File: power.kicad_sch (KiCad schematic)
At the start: 28 parts, among them J1 USBC, Q1 2N7002, SW3 PWR_ON, U2 LM3670MF, U5 MCP73831-3-OT, U6 MAX17043G+T

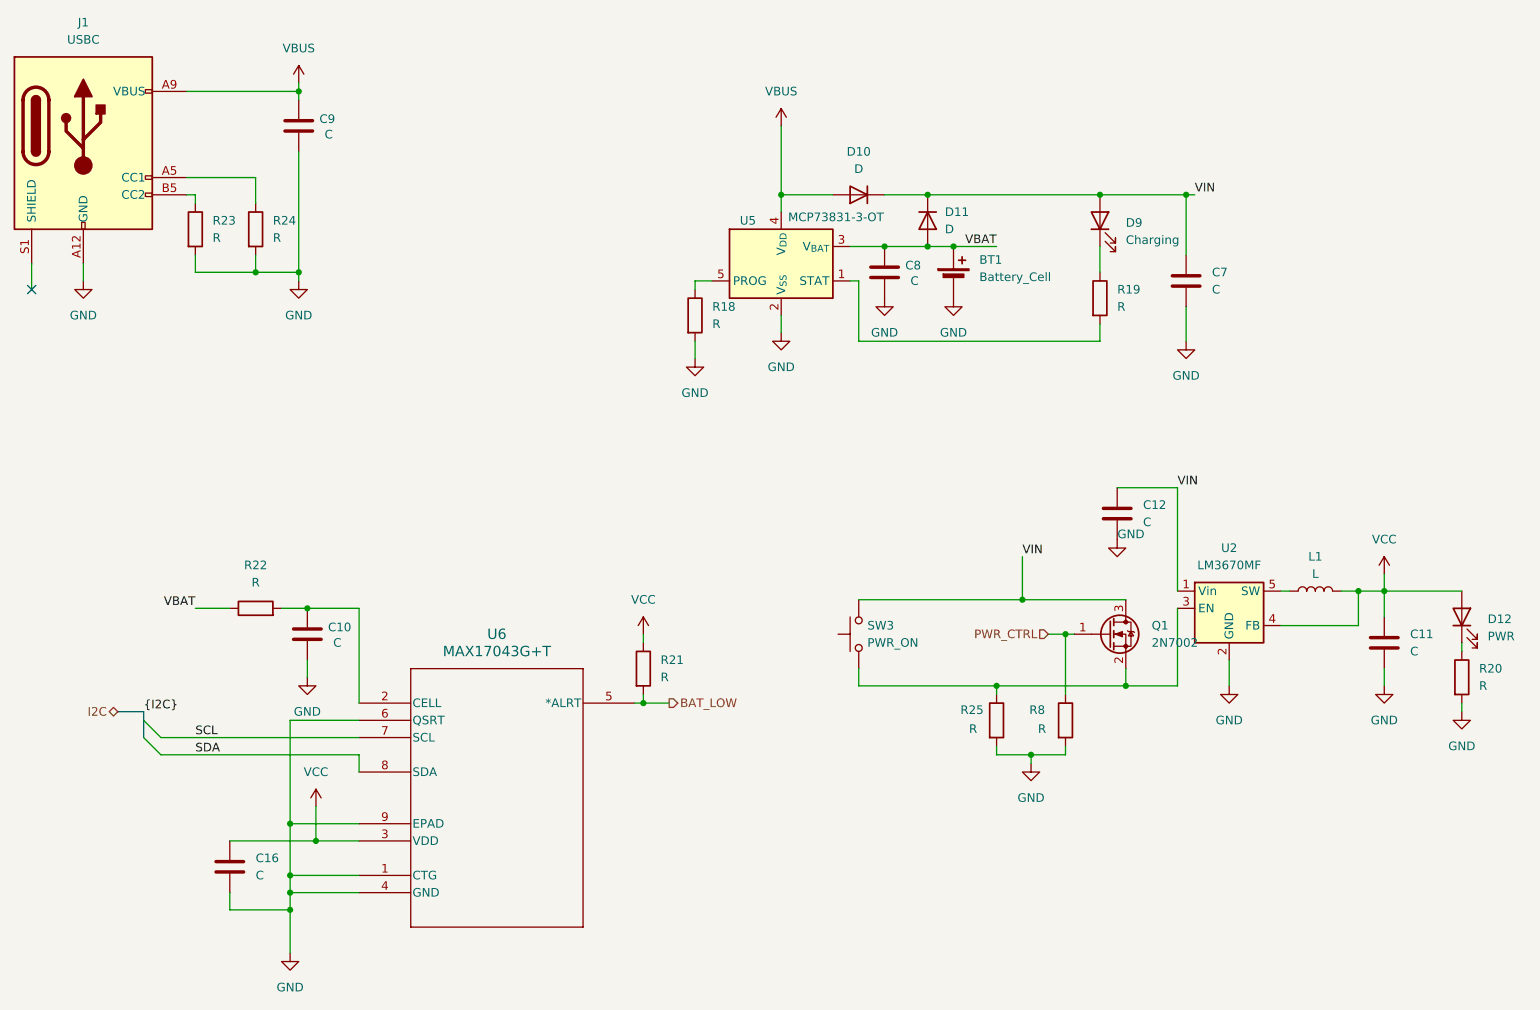
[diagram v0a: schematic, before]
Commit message: Power control using p-channel for switching
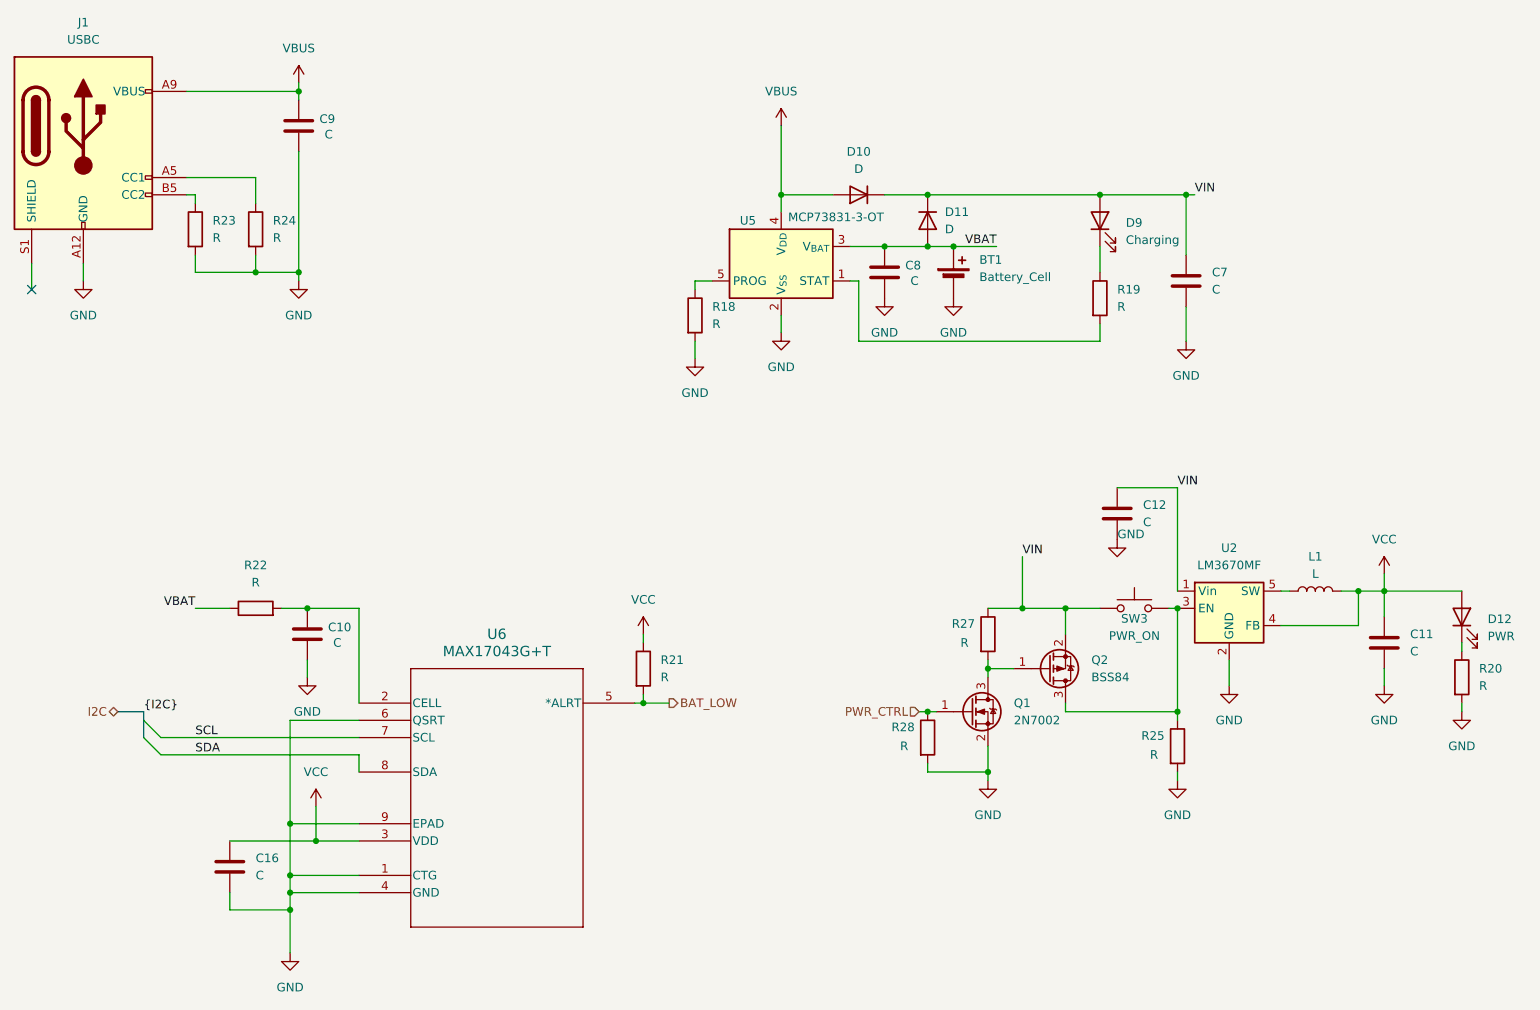
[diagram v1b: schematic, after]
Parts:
- removed R8: R, Resistor_SMD:R_0805_2012Metric_Pad1.20x1.40mm_HandSolder, symbol Device:R
- added Q2: BSS84, Package_TO_SOT_SMD:SOT-23, symbol Transistor_FET:BSS84
- added R27, R28: R, Resistor_SMD:R_0805_2012Metric_Pad1.20x1.40mm_HandSolder, symbol Device:R
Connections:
- net GND: now also Q1.2 (S), R28.2
- net PWR_CTRL: now also R28.1
- net VIN: now also SW3.1, Q2.2 (S), R27.1; no longer Q1.3 (D), SW3.2
- net at R25.1, U2.3 (EN): now also SW3.2, Q2.3 (D); no longer Q1.2 (S), SW3.1
- new net: Q1.3 (D), Q2.1 (G), R27.2
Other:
- moved on the sheet: Q1, R25, SW3

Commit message: Power component value assignment
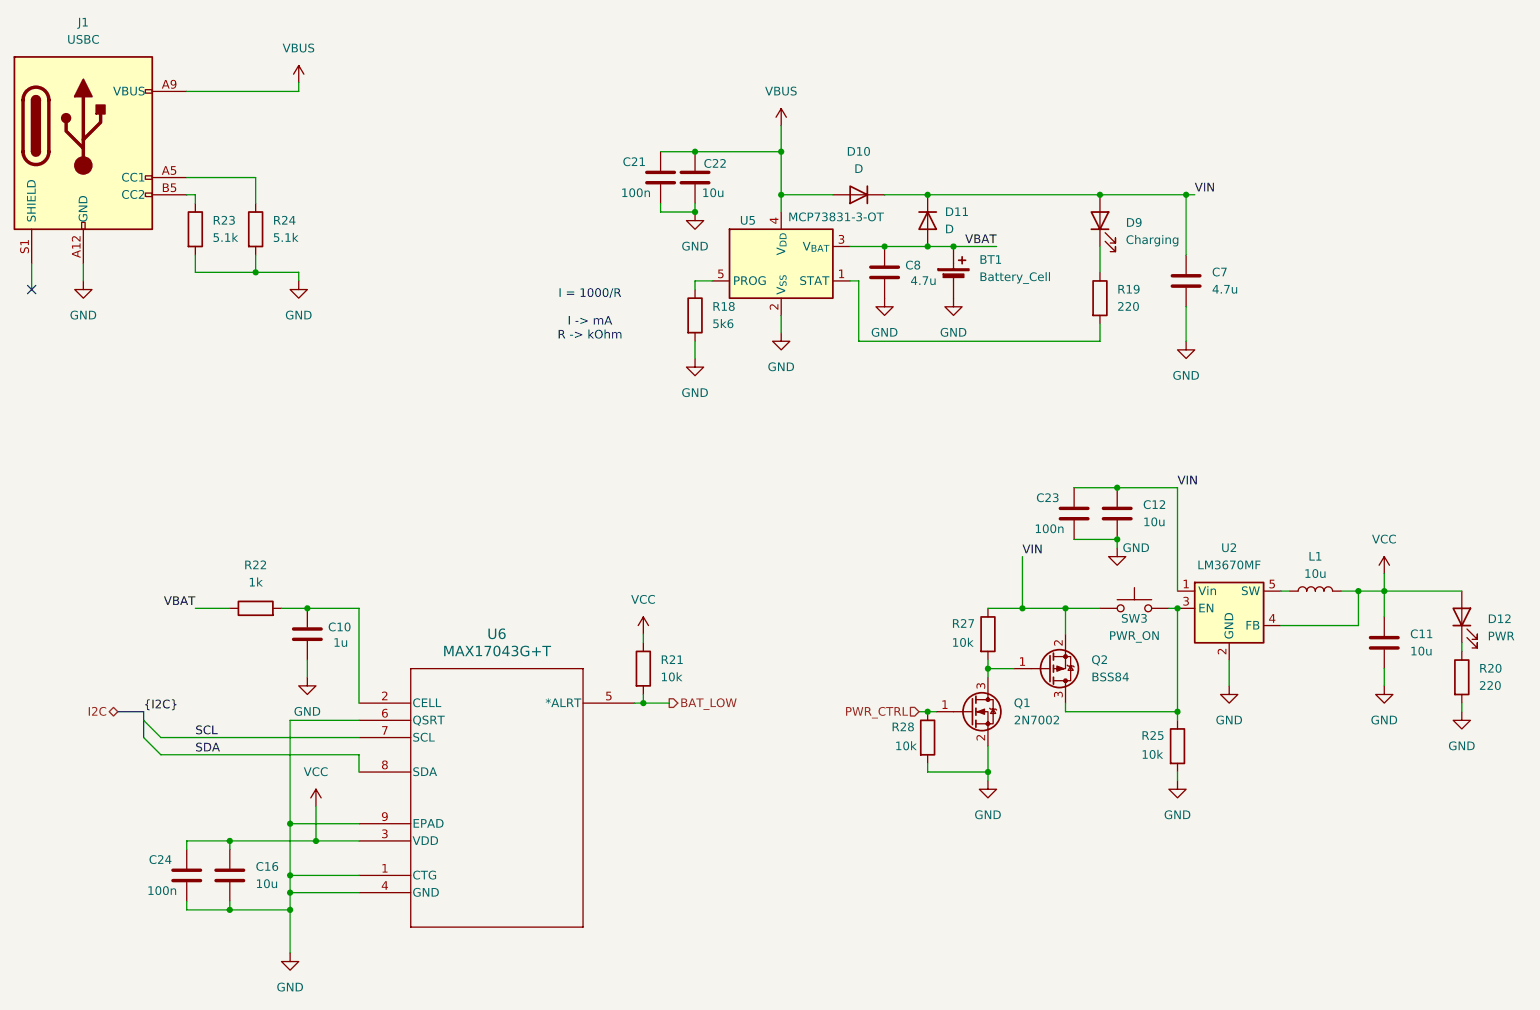
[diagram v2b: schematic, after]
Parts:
- removed C9: C, Capacitor_SMD:C_0805_2012Metric_Pad1.18x1.45mm_HandSolder, symbol Device:C
- added C21, C23, C24: 100n, Capacitor_SMD:C_0805_2012Metric_Pad1.18x1.45mm_HandSolder, symbol Device:C
- added C22: 10u, Capacitor_SMD:C_0805_2012Metric_Pad1.18x1.45mm_HandSolder, symbol Device:C
- C10: value C -> 1u
- C11, C12, C16: value C -> 10u
- C7, C8: value C -> 4.7u
- L1: value L -> 10u
- R18: value R -> 5k6
- R19, R20: value R -> 220
- R21, R25, R27, R28: value R -> 10k
- R22: value R -> 1k
- R23, R24: value R -> 5.1k
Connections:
- net GND: now also C21.2, C22.2, C23.2, C24.2
- net VBUS: now also C21.1, C22.1
- net VCC: now also C24.1
- net VIN: now also C23.1
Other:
- note added: "I = 1000/R I -> mA R -> kOhm"
- moved on the sheet: C16

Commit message: Decoupling capacitor change from 10u to 1u
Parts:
- C12, C16, C22: value 10u -> 1u
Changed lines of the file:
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@@
 			)
 		)
-		(property "Value" "10u"
+		(property "Value" "1u"
 			(at 140.716 65.786 0)
 			(effects
@@
 			)
 		)
-		(property "Value" "10u"
+		(property "Value" "1u"
 			(at 74.93 167.6399 0)
 			(effects
@@
 			)
 		)
-		(property "Value" "10u"
+		(property "Value" "1u"
 			(at 205.74 114.2999 0)
 			(effects

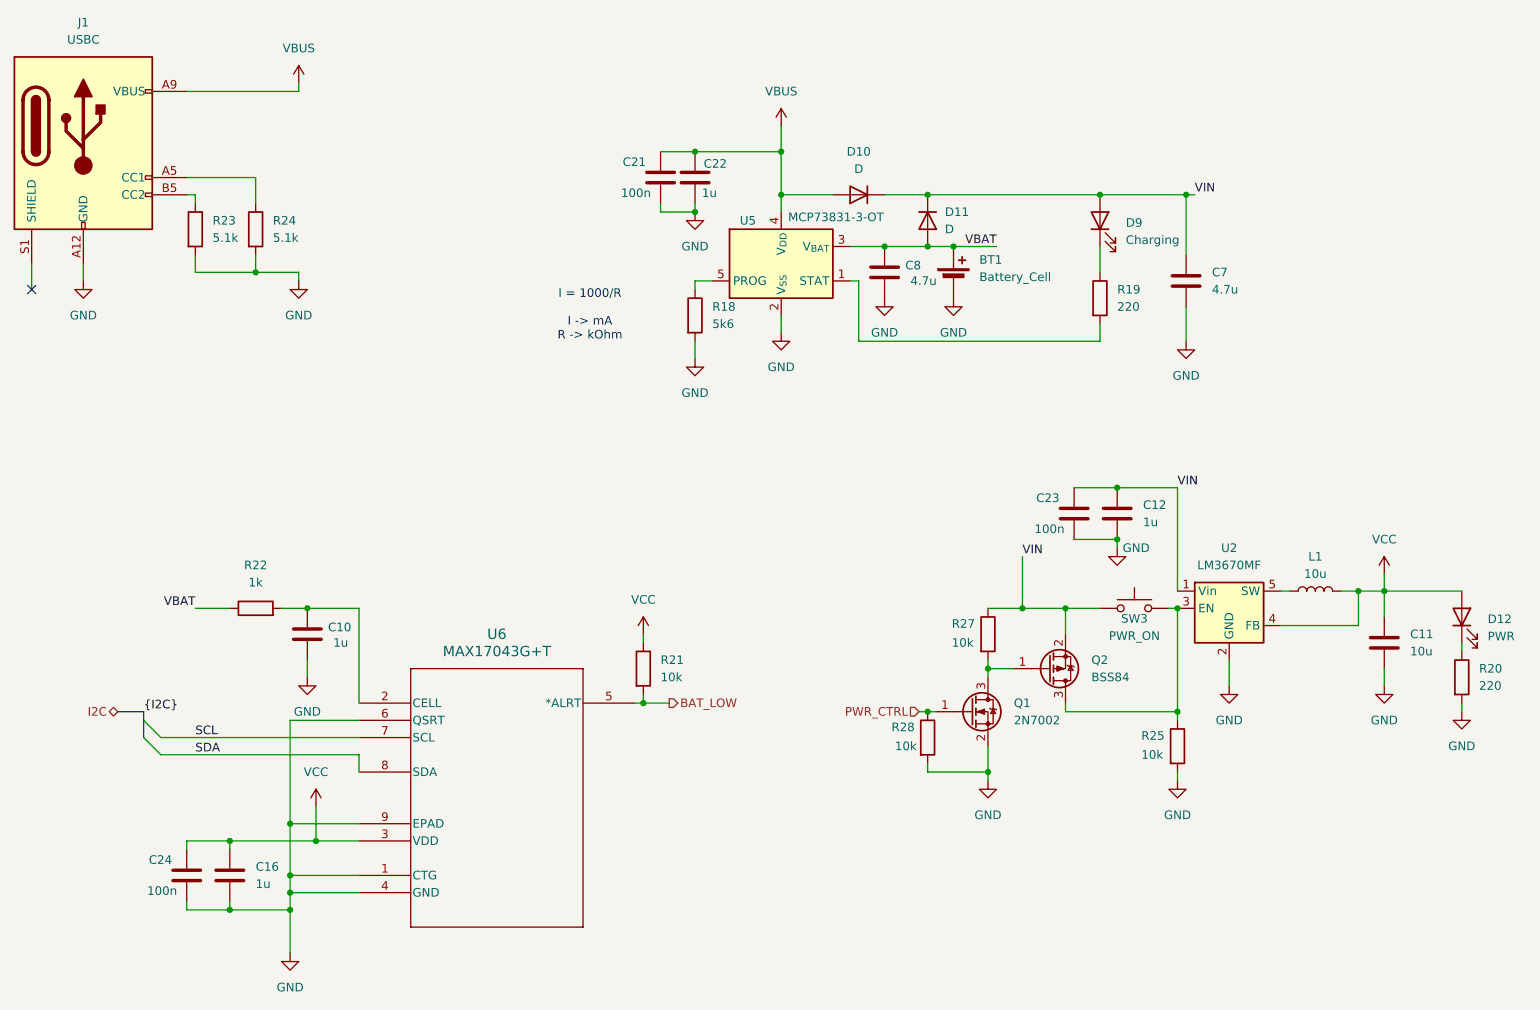
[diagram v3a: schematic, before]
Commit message: Resolve ERC warnings
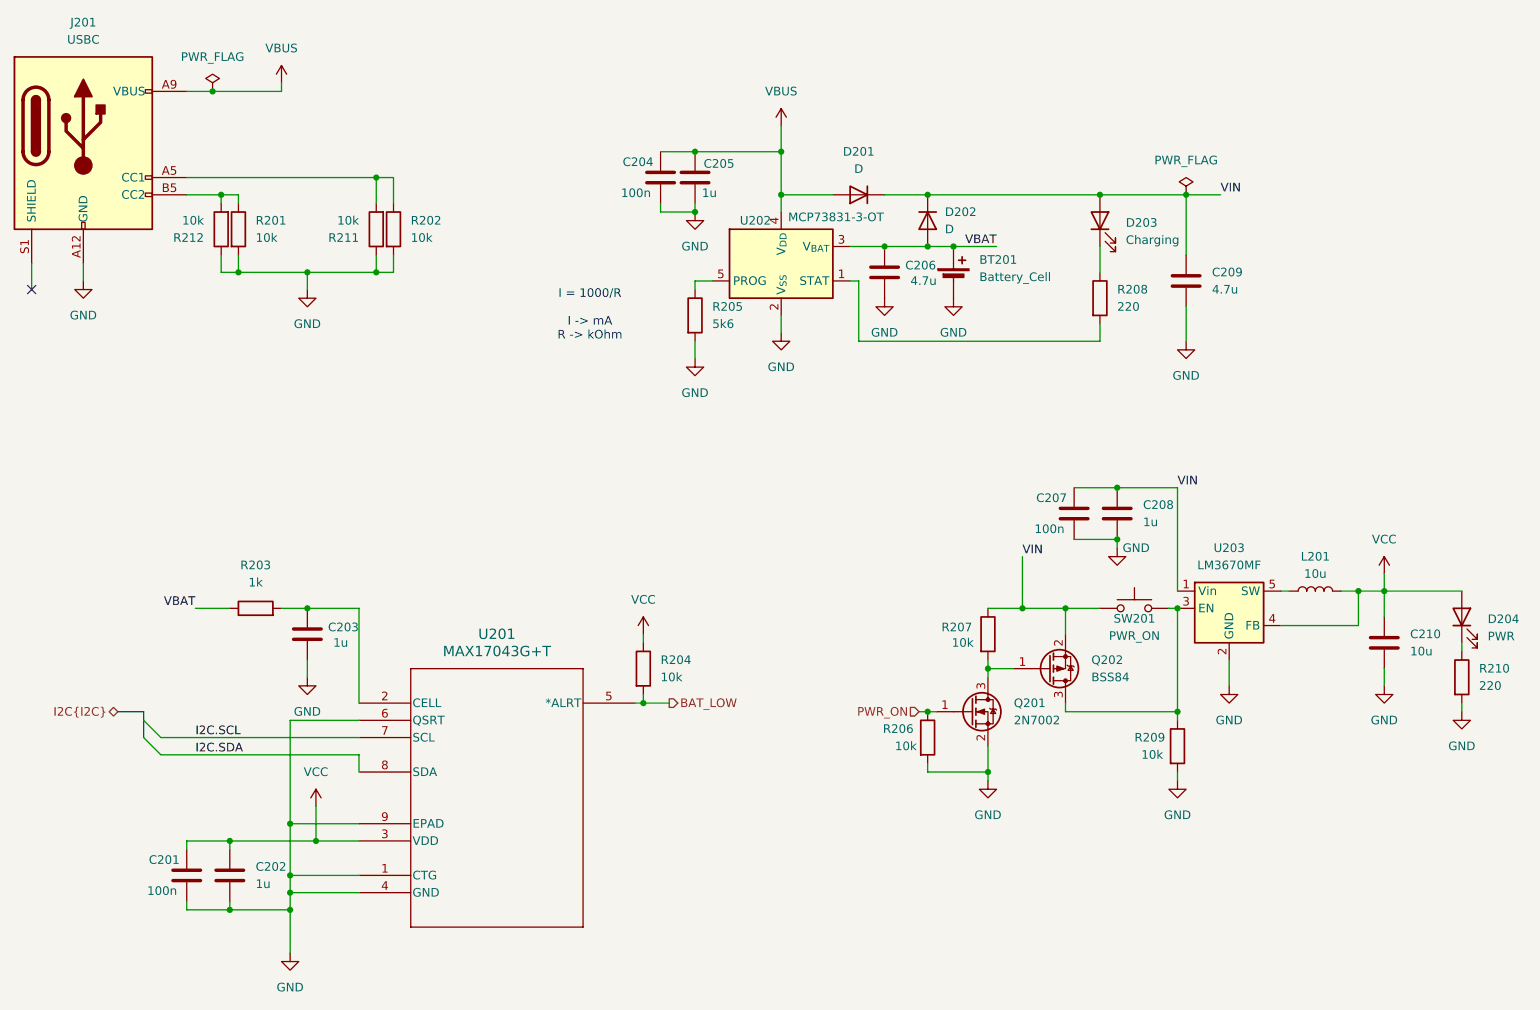
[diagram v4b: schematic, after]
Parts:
- added R211, R212: 10k, Resistor_SMD:R_0805_2012Metric_Pad1.20x1.40mm_HandSolder, symbol Device:R
- R201: renamed from R23; value 5.1k -> 10k
- R202: renamed from R24; value 5.1k -> 10k
- renumbered BT1 to BT201, C24 to C201, C16 to C202, C10 to C203, C21 to C204, C22 to C205, C8 to C206, C23 to C207, C12 to C208, C7 to C209, C11 to C210, D10 to D201, D11 to D202, D9 to D203, D12 to D204, J1 to J201, L1 to L201, Q1 to Q201, Q2 to Q202, R22 to R203, R21 to R204, R18 to R205, R28 to R206, R27 to R207, R19 to R208, R25 to R209, R20 to R210, SW3 to SW201, U6 to U201, U5 to U202, U2 to U203
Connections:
- net GND: now also R211.1, R212.1
- net at J201.A5 (CC1), R202.1: now also R211.2
- net at J201.B5 (CC2), R201.1: now also R212.2
- net PWR_CTRL renamed PWR_ON
- net SCL renamed I2C.SCL
- net SDA renamed I2C.SDA
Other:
- moved on the sheet: R201, R202

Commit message: Add Testpoints
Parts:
- added R213, R214: 1k, Resistor_SMD:R_0805_2012Metric_Pad1.20x1.40mm_HandSolder, symbol Device:R
- added TP1: VBUS, symbol Connector:TestPoint
- added TP2: VIN, symbol Connector:TestPoint
- added TP3: VBAT, symbol Connector:TestPoint
- added TP4: VCC, symbol Connector:TestPoint
- added TP5: PWR_ON, symbol Connector:TestPoint
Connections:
- net VBAT: now also TP3.1
- net VBUS: now also TP1.1
- net VCC: now also TP4.1
- net VIN: now also TP2.1
- net at R201.1, R212.2: now also R214.2; no longer J201.B5 (CC2)
- net at Q202.3 (D), R209.1, SW201.2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: now also TP5.1
- net at R202.1, R211.2: now also R213.2; no longer J201.A5 (CC1)
- new net: J201.A5 (CC1), R213.1
- new net: J201.B5 (CC2), R214.1
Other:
- moved on the sheet: R201, R202, R211, R212
